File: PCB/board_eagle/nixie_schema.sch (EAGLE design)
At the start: 82 parts, among them Q1 BC856B, Q2 IRF740S

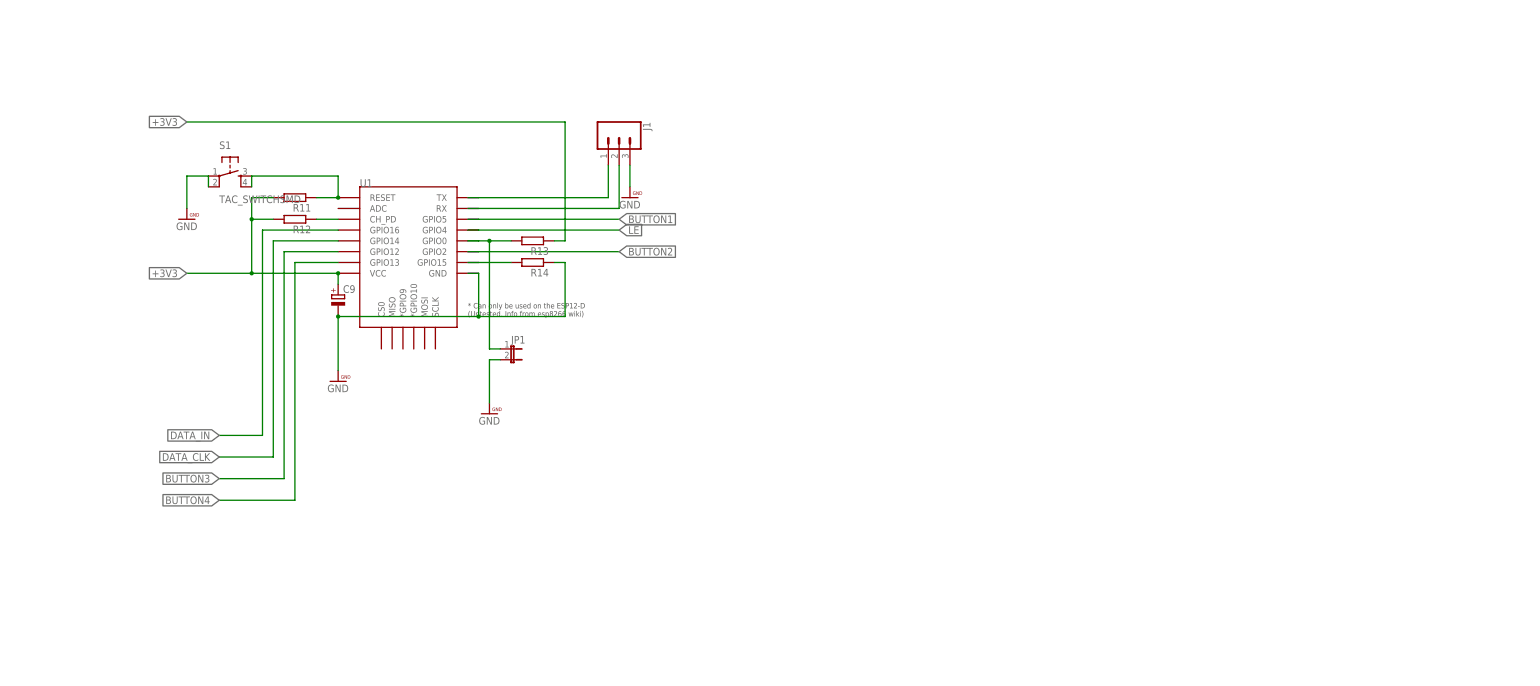
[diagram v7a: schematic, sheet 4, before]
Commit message: Added optional RTC module and cleaned up the schematic
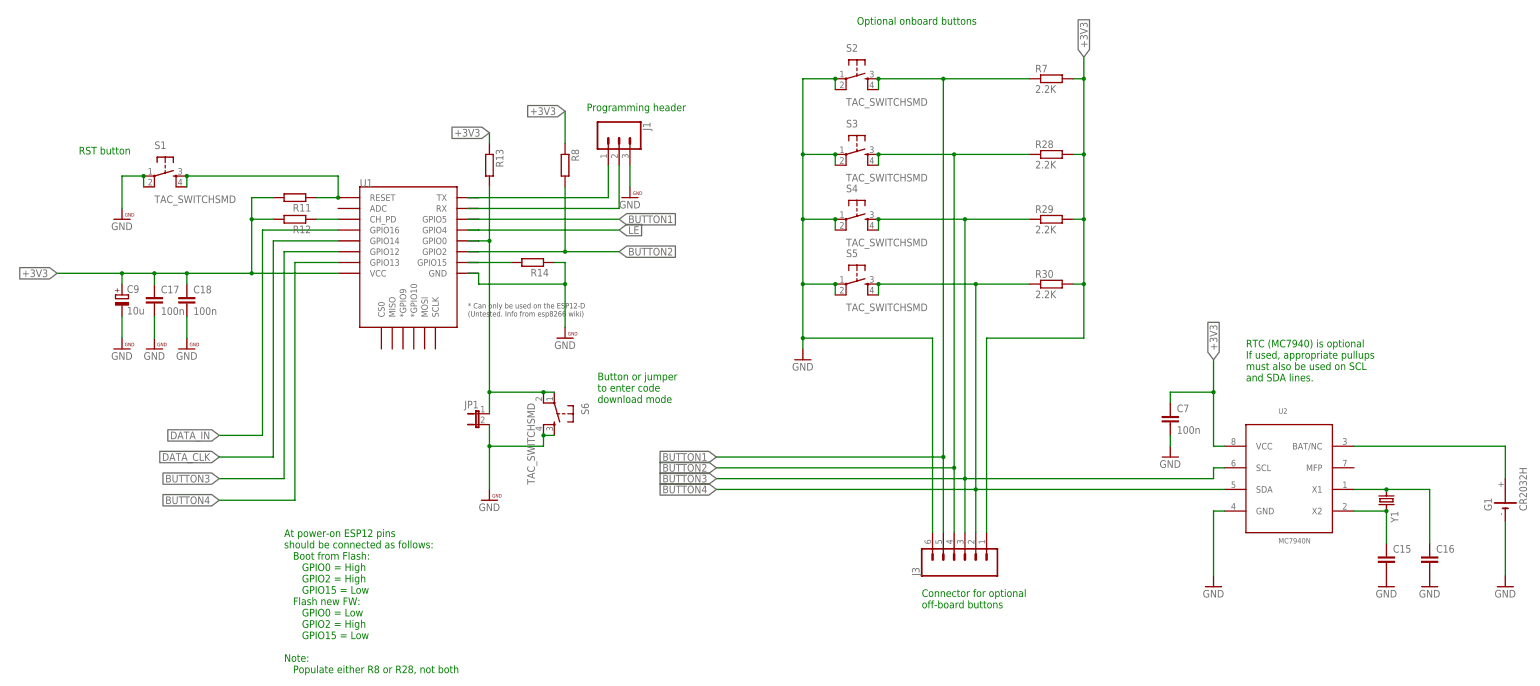
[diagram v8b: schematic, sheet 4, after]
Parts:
- removed J2: (no value), SparkFun-Connectors:CONN_06NO_SILK_FEMALE_PTH
- added C14, C17, C18, C7, C8: 100n, rcl:C-EUC0805
- added C15, C16: (no value), rcl:C-EUC0805
- added G1: CR2032H, battery:CR2032H
- added R8: (no value), resistor:R-EU_R0603
- added S6: TAC_SWITCHSMD, SparkFun-Retired:TAC_SWITCHSMD
- added U2: MC7940N, nixe_cmp:MC7940N
- added Y1: (no value), crystal:CRYSTALSM49
- C1, C3: device rcl:CPOL-EU140CLH-0810 -> rcl:C-EUC0805
- C10, C11, C4: device eagle-ltspice:C -> rcl:C-EUC0805
- C9: value (none) -> 10u
- R1, R2, R3, R4, R5, R6: value 2.21K -> 2.2k
- R28, R29, R30, R7: value 2.21K -> 2.2K
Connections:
- new net N$100: C15.1, U2.X2, Y1.2
- new net N$15: JP1.1, R13.2, S6.1, S6.2, U1.GPIO0
- new net N$99: C16.1, U2.X1, Y1.1
- net +3V3: now also C17.1, C18.1, R28.2, R29.2, R30.2, R7.2, R8.1, U2.VCC; no longer J2.1, S2.3, S3.3, S4.3, S5.3
- net BUTTON1: now also J3.5, R7.1, S2.3, S2.4; no longer J2.2, J3.2, R30.2, S5.1, S5.2
- net BUTTON2: now also J3.4, R28.1, R8.2, S3.3, S3.4; no longer J2.3, J3.3, R29.2, S4.1, S4.2
- net BUTTON3: now also J3.3, R29.1, S4.3, S4.4, U2.SCL; no longer J2.4, J3.4, R28.2, S3.1, S3.2
- net BUTTON4: now also J3.2, R30.1, S5.3, S5.4, U2.SDA; no longer J2.5, J3.5, R7.2, S2.1, S2.2
- net GND: now also C15.2, C16.2, C17.2, C18.2, C7.2, G1.-, S1.1, S2.1, S2.2, S3.1, S3.2, S4.1, S4.2, S5.1, S5.2, S6.3, S6.4, U2.GND; no longer C1.-, C10.2, C11.2, C3.-, C4.2, J2.6, R28.1, R29.1, R30.1, R7.1
- net N$12: no longer C4.1
- net N$14: now also S1.3
- net N$22: now also G1.+, U2.BAT/NC; no longer JP1.1, R13.2, U1.GPIO0
- net N$74: no longer C10.1
- net N$96: no longer C11.1
- net VCC: no longer C1.+, C3.+
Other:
- note added: "At power-on ESP12 pins should be connected as follows: Boot from Flash: GPIO0 = High GPIO2 = High GPIO15 = Low Flash new FW: GPIO0 = Low GPIO2 = High GPIO15 = Low Note: Populate either R8 or R28, not both"
- note added: "Button or jumper to enter code download mode"
- note added: "Connector for optional off-board buttons"
- note added: "Optional onboard buttons"
- note added: "Programming header"
- note added: "RST button"
- note added: "RTC (MC7940) is optional If used, appropriate pullups must also be used on SCL and SDA lines."
- moved on the sheet: C9, JP1, R13, R3, R6, S1
